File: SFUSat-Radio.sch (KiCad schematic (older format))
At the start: 10 parts, among them J1 SMA, P1 CONN_02X05, SW1 JS202011SCQN, U1 2N7002DW

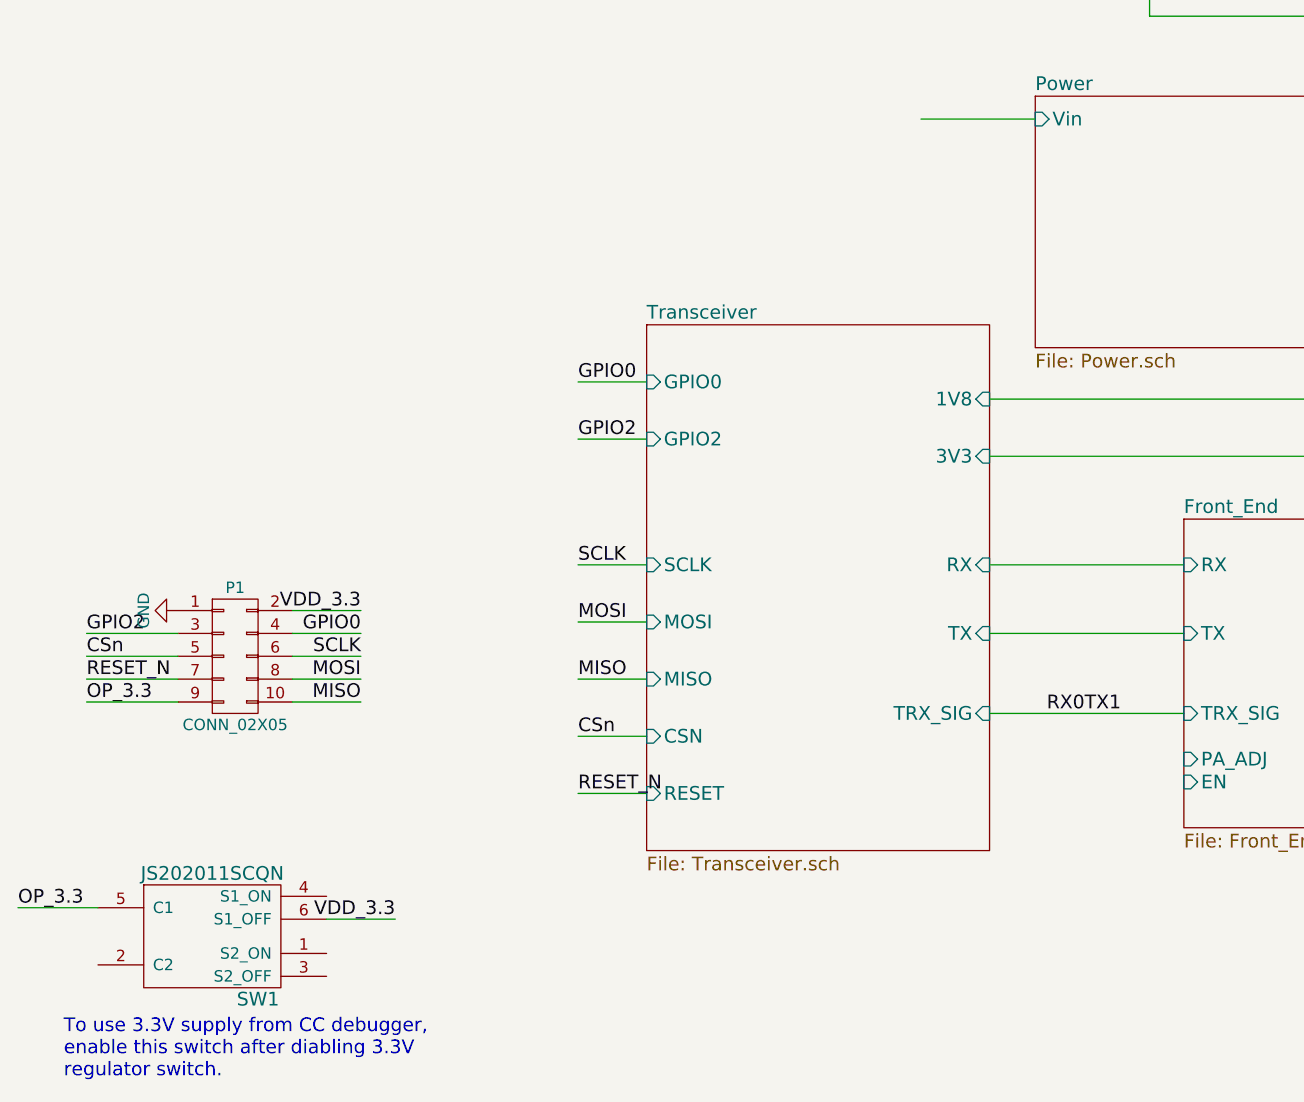
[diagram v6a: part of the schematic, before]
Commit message: added some test points
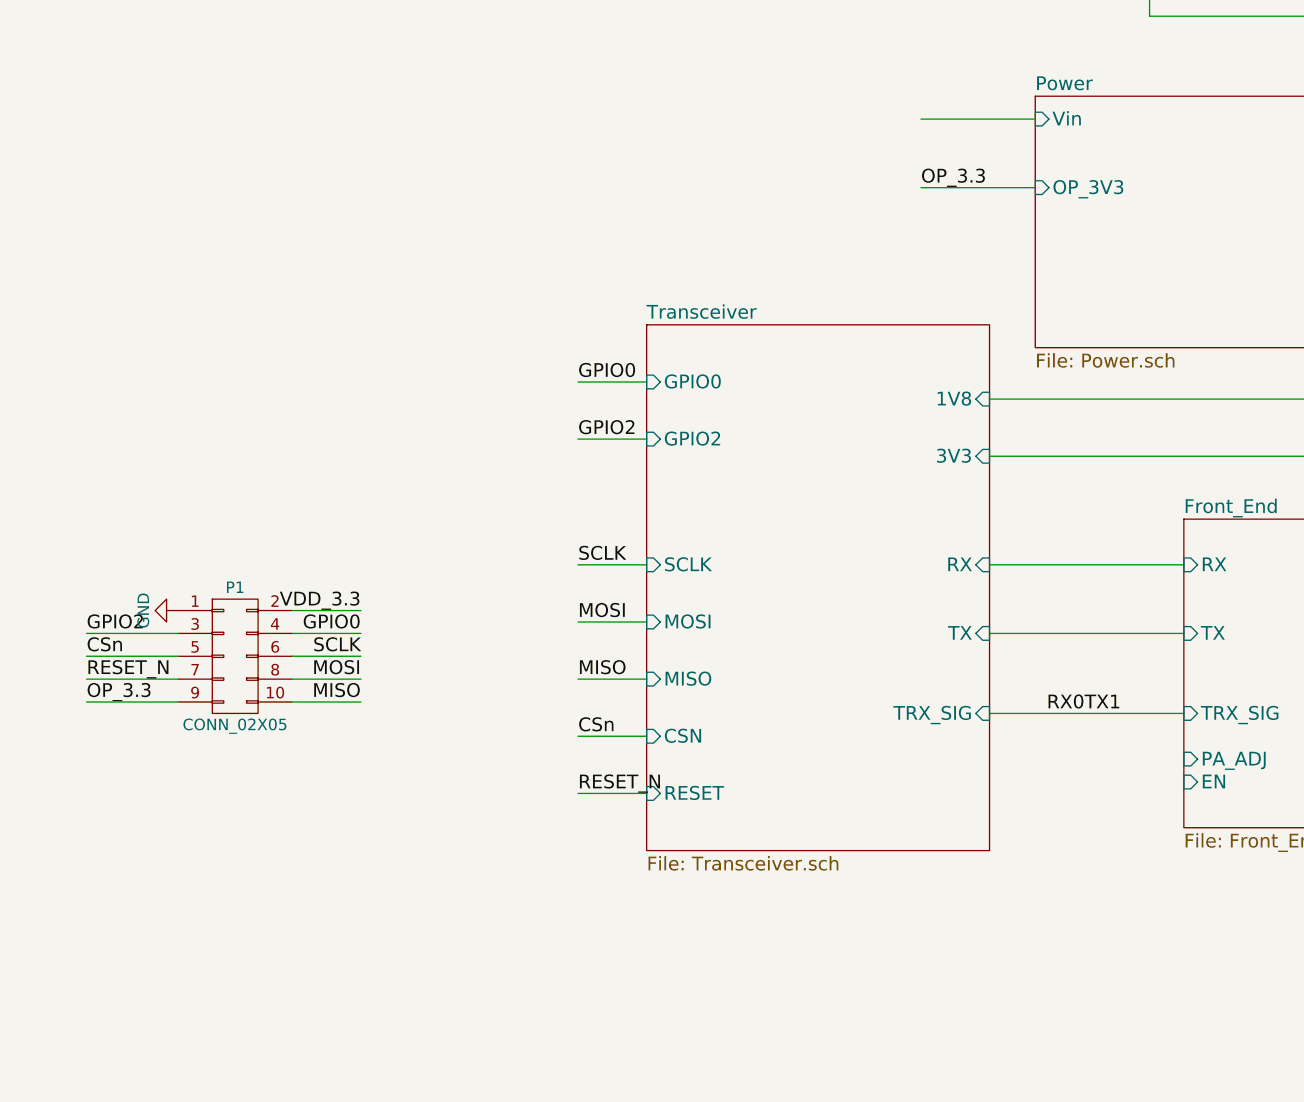
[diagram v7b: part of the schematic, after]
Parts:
- removed SW1: JS202011SCQN, SFUSat-Radio:JS2020_TH, symbol JS202011SCQN
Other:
- note removed: "To use 3.3V supply from CC debugger, \nenable this switch after diabling 3.3V \nregulator switch."
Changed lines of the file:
@@
 F4 "3V6" I R 6950 2800 60
 F5 "1V8" I R 6950 3300 60
+F6 "OP_3V3" I L 5400 2950 60
 $EndSheet
 Wire Wire Line
@@
 Text Label 2450 4800 2    60   ~ 0
 VDD_3.3
-Text Label 2600 6150 2    60   ~ 0
-VDD_3.3
-$Comp
-L JS202011SCQN SW1
-U 1 1 587DE706
-P 1800 6100
-F 0 "SW1" H 2000 5700 60  0000 C CNN
-F 1 "JS202011SCQN" H 1800 6250 60  0000 C CNN
-F 2 "SFUSat-Radio:JS2020_TH" H 1800 6100 60  0001 C CNN
-F 3 "" H 1800 6100 60  0000 C CNN
-	1    1800 6100
-	1    0    0    -1
-$EndComp
-Wire Wire Line
-	2300 6150 2600 6150
-Text Notes 1150 6850 0    60   ~ 0
-To use 3.3V supply from CC debugger, \nenable this switch after diabling 3.3V \nregulator switch.
 $Comp
 L 2N7002DW U1
@@
 Text Label 3400 5600 0    60   ~ 0
 RESET_N
-Wire Wire Line
-	1300 6100 950  6100
-Text Label 950  6100 0    60   ~ 0
-OP_3.3
 $Comp
 L SMA J1
@@
 	0    -1   -1   0
 $EndComp
+Wire Wire Line
+	5400 2950 4900 2950
+Text Label 4900 2950 0    60   ~ 0
+OP_3.3
 $EndSCHEMATC

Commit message: Checked changes from botched commit
-R5 and R6 are gone as desired
-C4 changed from 10 nF to 100 nF looks good
-Split up nets between pins 27 and 28 so each have their own dedicated
capacitor
-Added C9 to pin 28 and forward annotated it into the layout
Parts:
- D1, D2, D3: symbol LED -> LED-RESCUE-SFUSat-Radio
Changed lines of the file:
@@
 EESchema Schematic File Version 2
+LIBS:SFUSat-Radio-rescue
 LIBS:power
 LIBS:device
@@
 $EndComp
 $Comp
-L GND #PWR01
+L GND #PWR1
 U 1 1 587CE076
 P 1650 4800
-F 0 "#PWR01" H 1650 4550 50  0001 C CNN
+F 0 "#PWR1" H 1650 4550 50  0001 C CNN
 F 1 "GND" H 1650 4650 50  0000 C CNN
 F 2 "" H 1650 4800 50  0000 C CNN
@@
 $EndComp
 $Comp
-L LED D1
+L LED-RESCUE-SFUSat-Radio D1
 U 1 1 587E94F9
 P 6950 1250
@@
 $EndComp
 $Comp
-L LED D2
+L LED-RESCUE-SFUSat-Radio D2
 U 1 1 587EC634
 P 7250 1250
@@
 $EndComp
 $Comp
-L GND #PWR02
+L GND #PWR2
 U 1 1 587EE6E2
 P 6800 1550
-F 0 "#PWR02" H 6800 1300 50  0001 C CNN
+F 0 "#PWR2" H 6800 1300 50  0001 C CNN
 F 1 "GND" H 6800 1400 50  0000 C CNN
 F 2 "" H 6800 1550 50  0000 C CNN
@@
 $EndComp
 $Comp
-L GND #PWR03
+L GND #PWR3
 U 1 1 587EE79C
 P 6800 1750
-F 0 "#PWR03" H 6800 1500 50  0001 C CNN
+F 0 "#PWR3" H 6800 1500 50  0001 C CNN
 F 1 "GND" H 6800 1600 50  0000 C CNN
 F 2 "" H 6800 1750 50  0000 C CNN
@@
 	7250 1650 7250 1450
 $Comp
-L LED D3
+L LED-RESCUE-SFUSat-Radio D3
 U 1 1 587F1822
 P 7550 1250
@@
 $EndComp
 $Comp
-L GND #PWR04
+L GND #PWR4
 U 1 1 587F1A5F
 P 7550 1450
-F 0 "#PWR04" H 7550 1200 50  0001 C CNN
+F 0 "#PWR4" H 7550 1200 50  0001 C CNN
 F 1 "GND" H 7550 1300 50  0000 C CNN
 F 2 "" H 7550 1450 50  0000 C CNN
@@
 $EndComp
 $Comp
-L GND #PWR05
+L GND #PWR5
 U 1 1 5883A521
 P 9700 5050
-F 0 "#PWR05" H 9700 4800 50  0001 C CNN
+F 0 "#PWR5" H 9700 4800 50  0001 C CNN
 F 1 "GND" H 9700 4900 50  0000 C CNN
 F 2 "" H 9700 5050 50  0000 C CNN
